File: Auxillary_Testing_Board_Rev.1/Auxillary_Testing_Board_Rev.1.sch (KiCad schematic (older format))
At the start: 34 parts, among them SW1 SW_Push, SW10 SW_Push, SW11 SW_Push, SW12 SW_Push, SW13 SW_Push, SW14 SW_Push, SW15 SW_Push, SW16 SW_Push, SW17 SW_Push, SW18 SW_Push, SW19 SW_Push, SW2 SW_Push, SW20 SW_Push, SW21 SW_Push, SW22 SW_Push, SW23 SW_Push, SW24 SW_Push, SW25 SW_Push, SW26 SW_Push, SW27 SW_Push, SW28 SW_SPDT, SW3 SW_Push, SW4 SW_Push, SW5 SW_Push, SW6 SW_Push, SW7 SW_Push, SW8 SW_Push, SW9 SW_Push, U1 TM4C129E_Launchpad, U2 OKI, U3 TM4C129E_Launchpad

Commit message: finished layout maybe
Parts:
- C1, C2: value C -> 10uF; footprint (none) -> Capacitor_SMD:C_0603_1608Metric_Pad1.05x0.95mm_HandSolder
- Conn1: footprint (none) -> MRDT_Connectors:Anderson_2_Horizontal_Side_by_Side
- SW1, SW10, SW11, SW12, SW13, SW14, SW15, SW16, SW17, SW18, SW19, SW2, SW20, SW21, SW22, SW23, SW24, SW25, SW26, SW27, SW3, SW4, SW5, SW6, SW7, SW8, SW9: footprint (none) -> Button_Switch_SMD:SW_SPST_TL3305A
- SW28: footprint (none) -> Button_Switch_THT:SW_CuK_JS202011AQN_DPDT_Angled
- U1, U3: footprint (none) -> MRDT_Shields:Auxillary_Testing_Board
- U2: footprint (none) -> MRDT_Devices:OKI_Horizontal
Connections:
- net Fluid_1: now also U1.PC5 (A1_4); no longer U1.PE4 (A1_2)
- net Fluid_3: now also U1.PE4 (A1_2); no longer U1.PC5 (A1_4)
- net Forearm_Clockwise: now also U3.PE0 (B1_3); no longer U3.PC4 (A1_3)
- net Forearm_Counter_Clockwise: now also U3.PE1 (B1_4); no longer U3.PE4 (A1_2)
- net Geneva_Clockwise: now also U1.PP5 (D2_3); no longer U1.PP2 (D1_10)
- net Geneva_Counter_Clockwise: now also U1.PP2 (D1_10); no longer U1.PP5 (D2_3)
- net Gripper_Open: now also U3.PK5 (C2_3); no longer U3.PP5 (D2_3)
- net Laser: now also U3.PL3 (C1_10); no longer U3.PN2 (D1_8)
- net Nozzle_Down: now also U1.PN3 (D1_9); no longer U1.PN2 (D1_8)
- net Nozzle_Up: now also U1.PN2 (D1_8); no longer U1.PN3 (D1_9)
- net Spectrometer_Down: now also U1.PH3 (D1_4); no longer U1.PH2 (D1_3)
- net Spectrometer_Up: now also U1.PH2 (D1_3); no longer U1.PH3 (D1_4)
- net Vacuum_fwd: now also U1.PE5 (A1_6); no longer U1.PC6 (A1_5)
- net Vacuum_rvs: now also U1.PC6 (A1_5); no longer U1.PE5 (A1_6)
- net Wrist_Clock: now also U3.PL2 (C1_9); no longer U3.PN3 (D1_9)
- net Wrist_Counter_Clock: now also U3.PL1 (C1_8); no longer U3.PP2 (D1_10)
- no-connect marks 120 -> 117
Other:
- note added: "Arm Tiva(back)"
- note added: "Science Tiva(front)"
- note removed: "Arm Tiva"
- note removed: "Science Tiva"

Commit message: Added LEDs to the schematic
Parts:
- removed SW28: SW_SPDT, Button_Switch_THT:SW_CuK_JS202011AQN_DPDT_Angled, symbol Switch:SW_SPDT
- added D1, D10, D11, D12, D13, D14, D15, D16, D17, D18, D19, D2, D20, D21, D22, D23, D24, D3, D4, D5, D6, D7, D8, D9: LED, LED_SMD:LED_0603_1608Metric_Pad1.05x0.95mm_HandSolder, symbol Device:LED
- added R1, R10, R11, R12, R13, R14, R15, R16, R17, R18, R19, R2, R20, R21, R22, R23, R24, R3, R4, R5, R6, R7, R8, R9: R, Resistor_SMD:R_0603_1608Metric_Pad1.05x0.95mm_HandSolder, symbol Device:R
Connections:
- net +3V3: now also R23.1, R5.1
- net Base_Left: now also U3.PQ0 (A2_7); no longer U3.PP0 (A2_3)
- net Base_Right: now also U3.PP4 (A2_8); no longer U3.PP1 (A2_4)
- net Elbow_Down: now also U3.PP1 (A2_4); no longer U3.PP4 (A2_8)
- net Elbow_Up: now also U3.PP0 (A2_3); no longer U3.PQ0 (A2_7)
- net GND: now also D1.1 (K), D10.1 (K), D11.1 (K), D12.1 (K), D13.1 (K), D14.1 (K), D15.1 (K), D16.1 (K), D17.1 (K), D18.1 (K), D19.1 (K), D2.1 (K), D20.1 (K), D21.1 (K), D22.1 (K), D23.1 (K), D24.1 (K), D3.1 (K), D4.1 (K), D5.1 (K), D6.1 (K), D7.1 (K), D8.1 (K), D9.1 (K)
- net Gripper_Close: now also U3.PL2 (C1_9); no longer U3.PQ2 (D2_6)
- net Gripper_Open: now also U3.PL1 (C1_8); no longer U3.PK5 (C2_3)
- net Wrist_Clock: now also U3.PQ2 (D2_6); no longer U3.PL2 (C1_9)
- net Wrist_Counter_Clock: now also U3.PK5 (C2_3); no longer U3.PL1 (C1_8)
- net Connection_Ind: now reaches U1.PE3 (B1_6)
- net Connection_Ind: now also U3.PE3 (B1_6), R24.1, R6.1
- net Nozzle_Down_Ind: now reaches U1.PL4 (C1_5)
- net Nozzle_Down_Ind: now also R2.1
- net Nozzle_Up_Ind: now reaches U1.PL5 (C1_6)
- net Nozzle_Up_Ind: now also R1.1
- net Spectrometer_Down_Ind: now reaches U1.PD0 (D1_7)
- net Spectrometer_Down_Ind: now also R3.1
- net Spectrometer_Up_Ind: now reaches U1.PD1 (D1_6)
- net Spectrometer_Up_Ind: now also R4.1
- net Gripper_Open_Ind: now reaches U3.PF2 (C1_2)
- net Gripper_Open_Ind: now also R16.1
- net Gripper_Close_Ind: now reaches U3.PF3 (C1_3)
- net Gripper_Close_Ind: now also R15.1
- net Forearm_Counter_Clockwise_Ind: now reaches U3.PG0 (C1_4)
- net Forearm_Counter_Clockwise_Ind: now also R14.1
- net Forearm_Clockwise_Ind: now reaches U3.PL0 (C1_7)
- net Forearm_Clockwise_Ind: now also R13.1
- net Base_Left_Ind: now reaches U3.PB4 (B2_3)
- net Base_Left_Ind: now also R17.1
- net Base_Right_Ind: now reaches U3.PB5 (B2_4)
- net Base_Right_Ind: now also R18.1
- net Elbow_Up_Ind: now reaches U3.PK0 (B2_5)
- net Elbow_Up_Ind: now also R19.1
- net Elbow_Down_Ind: now reaches U3.PK1 (B2_6)
- net Elbow_Down_Ind: now also R20.1
- net Base_Up_Ind: now reaches U3.PK2 (B2_7)
- net Base_Up_Ind: now also R21.1
- net Base_Down_Ind: now reaches U3.PK3 (B2_8)
- net Base_Down_Ind: now also R22.1
- net Laser_Ind: now reaches U3.PG1 (C2_1)
- net Laser_Ind: now also R8.1
- net Solenoid_Ind: now reaches U3.PH0 (C2_7)
- net Solenoid_Ind: now also R12.1
- net Wrist_Down_Ind: now reaches U3.PH1 (C2_8)
- net Wrist_Down_Ind: now also R11.1
- net Wrist_Counter_Clock_Ind: now reaches U3.PK4 (C2_2)
- net Wrist_Counter_Clock_Ind: now also R7.1
- net Wrist_Up_Ind: now reaches U3.PK6 (C2_9)
- net Wrist_Up_Ind: now also R10.1
- net Wrist_Clock_Ind: now reaches U3.PK7 (C2_10)
- net Wrist_Clock_Ind: now also R9.1
- net Mode_Toggle: no longer names the net of U1.PF1 (C1_1)
- new net: D7.2 (A), R7.2
- new net: D8.2 (A), R8.2
- new net: D9.2 (A), R9.2
- new net: D11.2 (A), R11.2
- new net: D12.2 (A), R12.2
- new net: D13.2 (A), R13.2
- new net: D14.2 (A), R14.2
- new net: D15.2 (A), R15.2
- new net: D16.2 (A), R16.2
- new net: D18.2 (A), R18.2
- new net: D19.2 (A), R19.2
- new net: D20.2 (A), R20.2
- new net: D21.2 (A), R21.2
- new net: D22.2 (A), R22.2
- new net: D10.2 (A), R10.2
- new net: D17.2 (A), R17.2
- new net: D6.2 (A), R6.2
- new net: D5.2 (A), R5.2
- new net: D2.2 (A), R2.2
- new net: D3.2 (A), R3.2
- new net: D4.2 (A), R4.2
- new net: D1.2 (A), R1.2
- new net: D24.2 (A), R24.2
- new net: D23.2 (A), R23.2
- no-connect marks 117 -> 96
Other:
- note added: "Arm Indicators"
- note added: "General Indicators"
- note added: "Science Indicators"
- note removed: "Toggle"
- moved on the sheet: C1, C2, Conn1A, Conn1C, SW1, SW10, SW11, SW2, SW3, SW4, SW5, SW6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

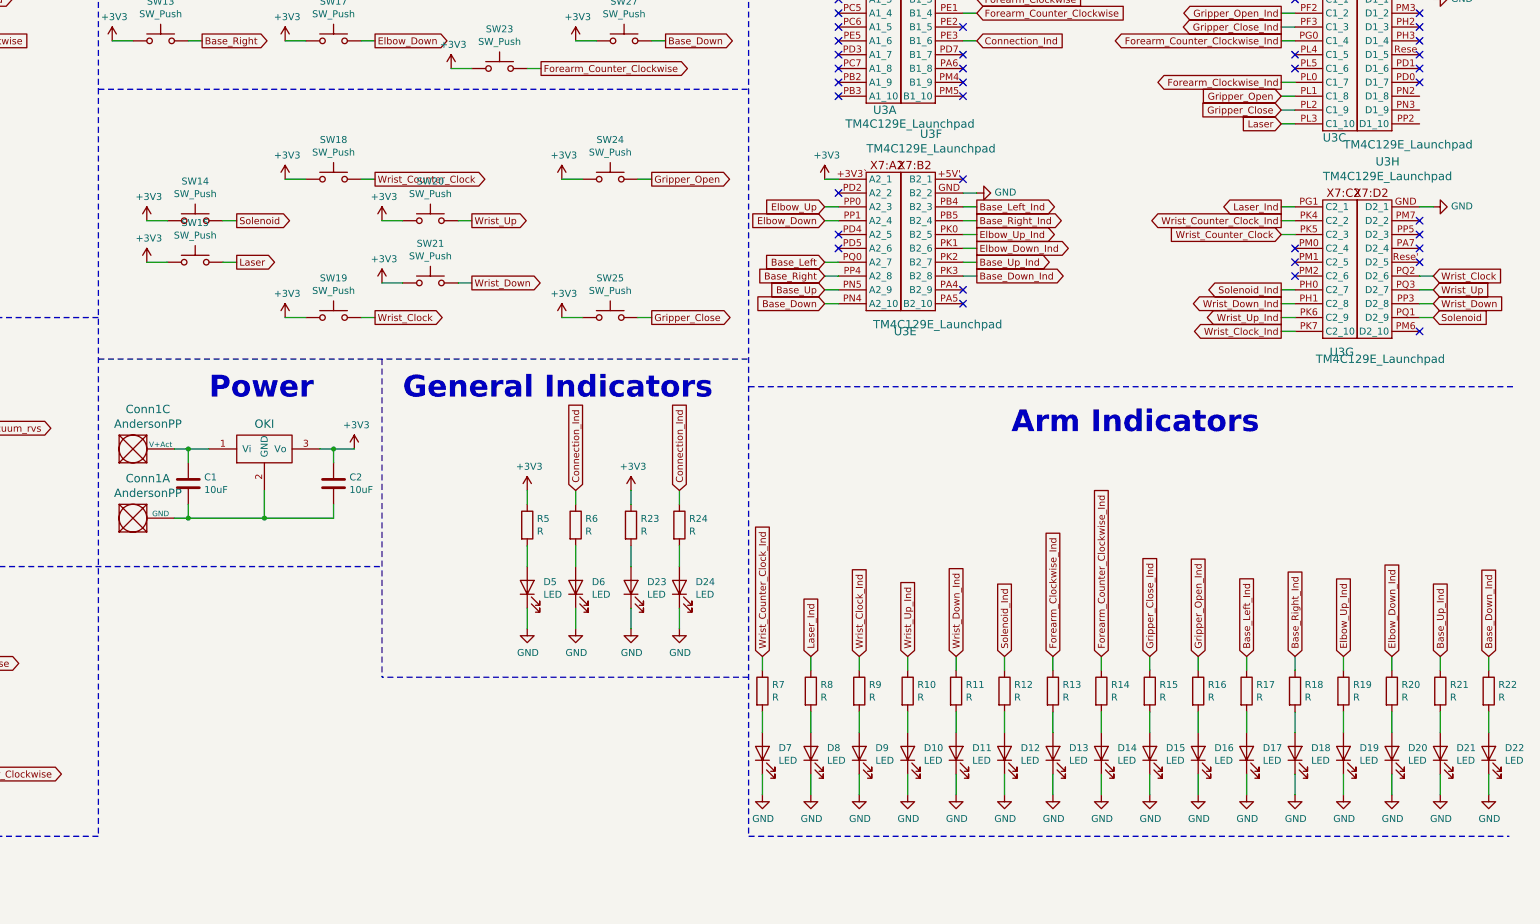
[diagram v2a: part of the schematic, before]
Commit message: layout routed, just need to make it look good
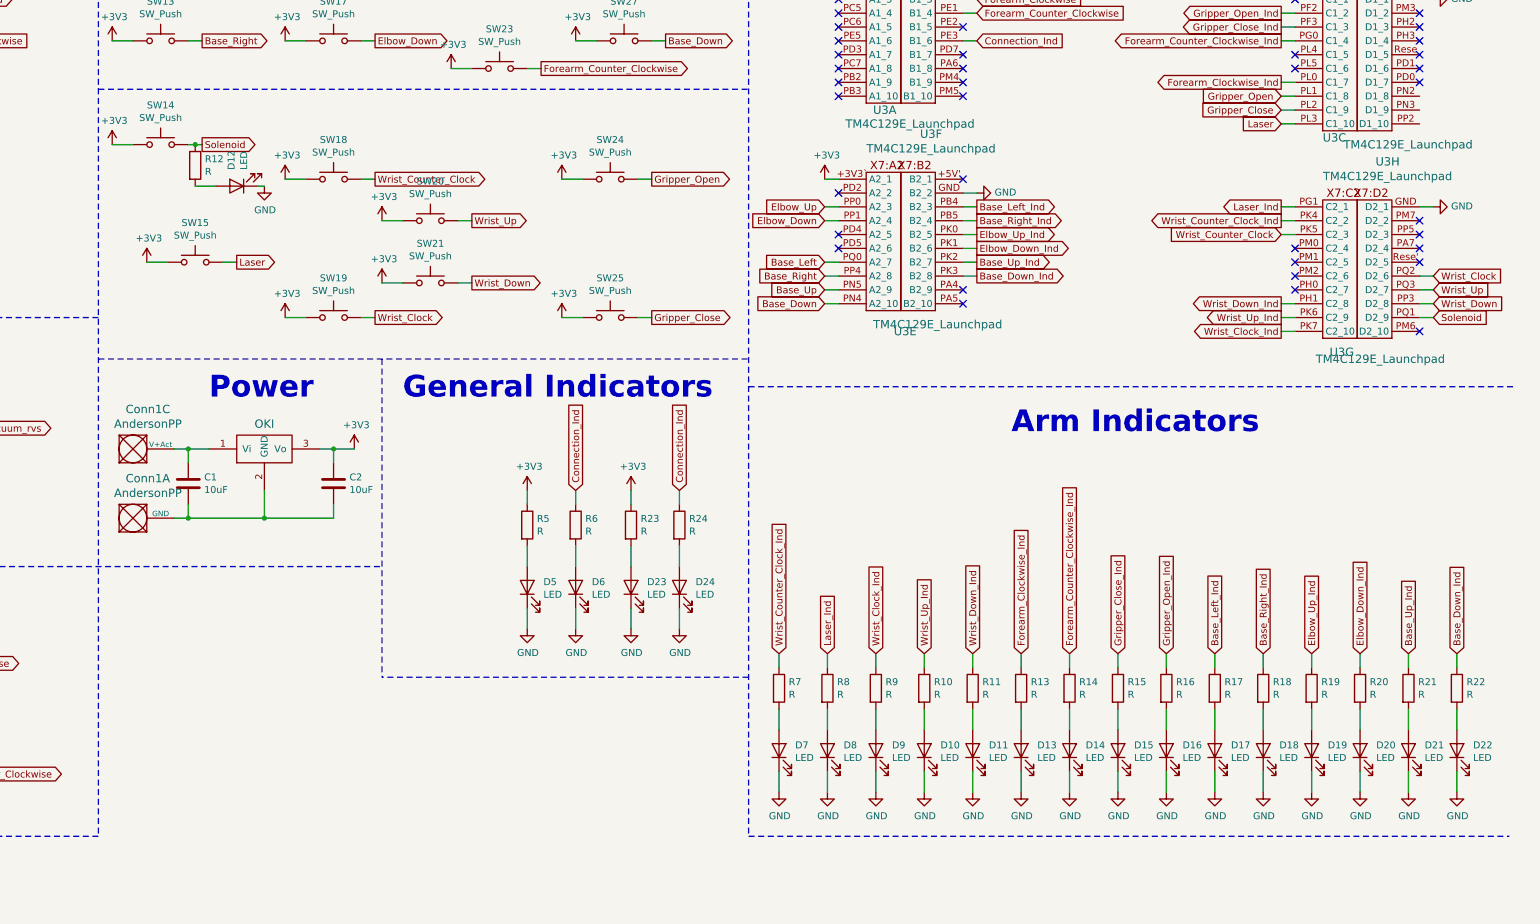
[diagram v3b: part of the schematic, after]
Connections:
- net Solenoid: now also R12.1
- net Solenoid_Ind: no longer names the net of U3.PH0 (C2_7)
- net Solenoid_Ind: no longer R12.1
- no-connect marks 96 -> 97
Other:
- moved on the sheet: D10, D11, D12, D13, D14, D15, D16, D17, D18, D19, D20, D21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
